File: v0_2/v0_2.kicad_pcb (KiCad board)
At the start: 2 copper layers, 36 x 70 mm, 46 parts, among them IC1 RASPBERRY_PI_PICO_W, IC2 BH1750FVI-TR, IC3 AP2138N-3.3TRG1, J1 S2B-PH-SM4-TB_LF__SN_, J2 HYCW110-TF10-180B, J3 Conn_01x09_Pin, Q1 DMG2301L-7, Q2 DMG2301L-7, Q3 DMG2301L-7, Q4 DMN3731U-13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

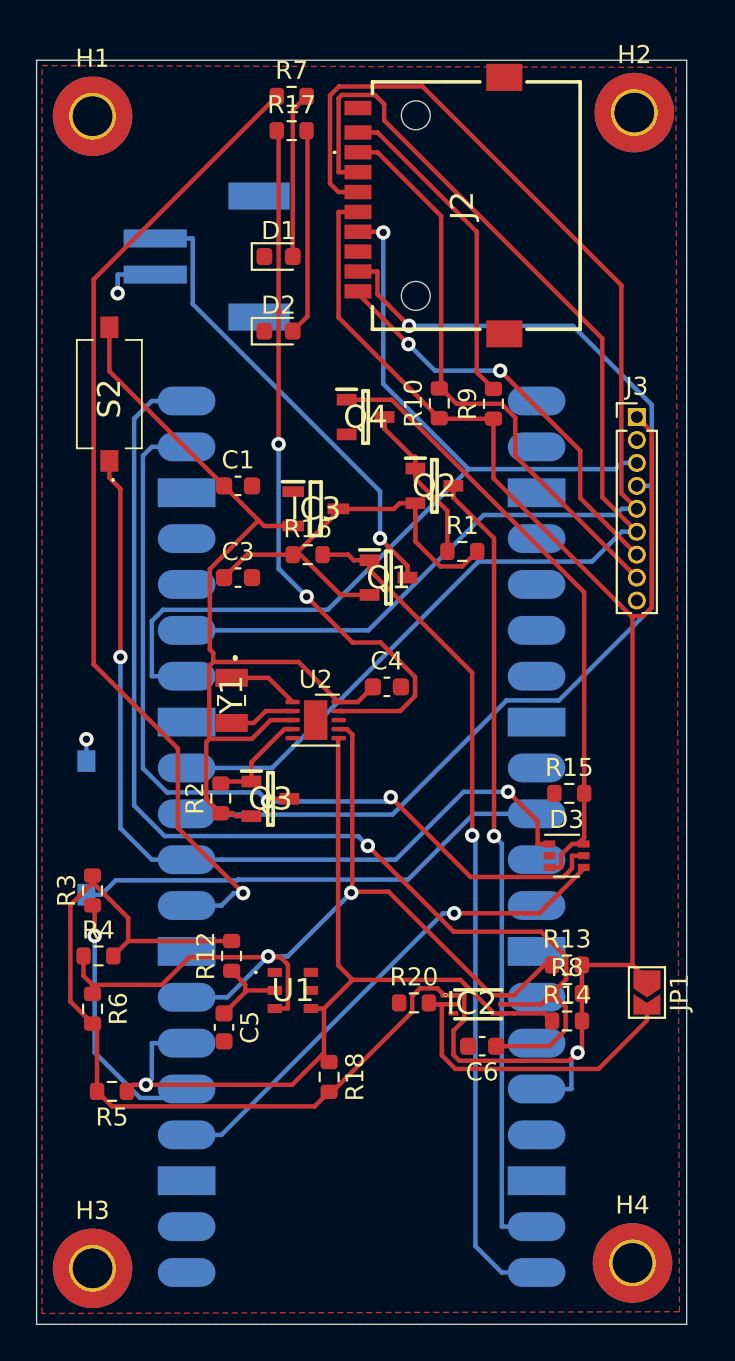
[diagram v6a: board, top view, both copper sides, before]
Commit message: rename i2c and add button
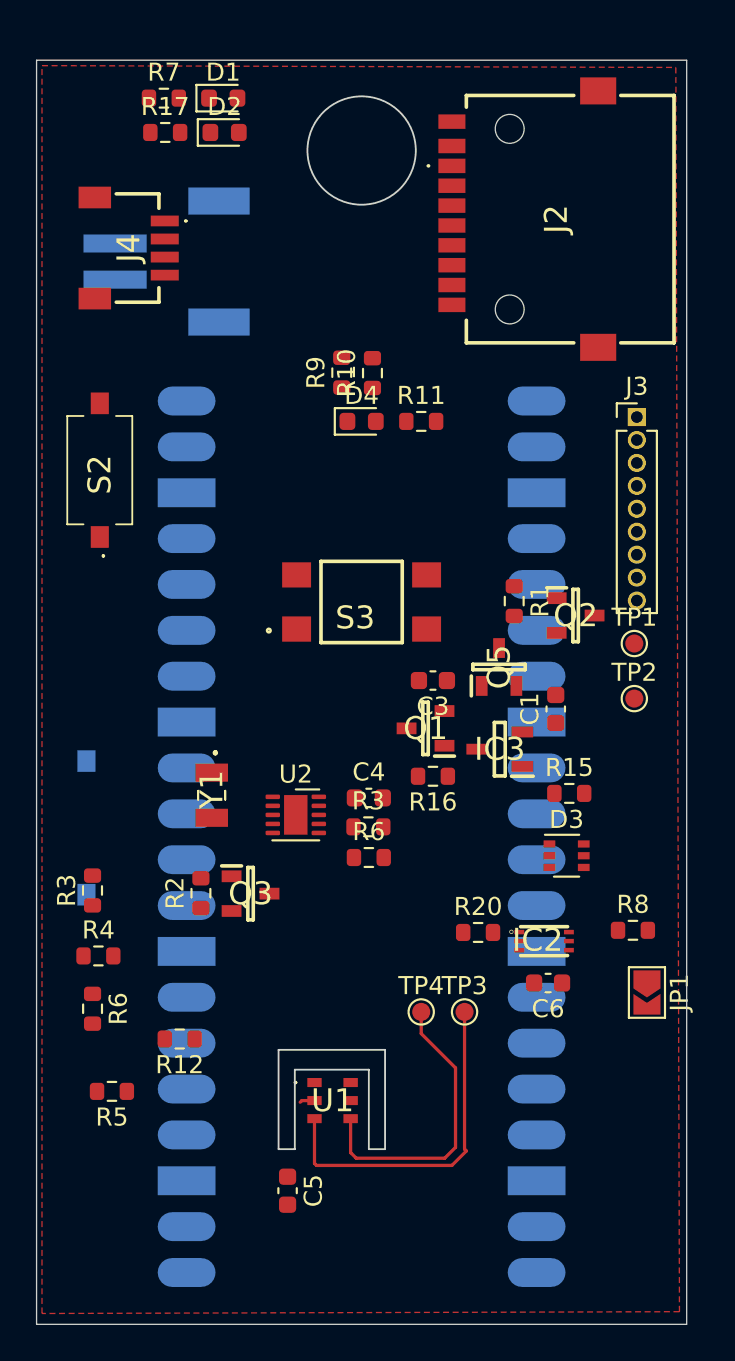
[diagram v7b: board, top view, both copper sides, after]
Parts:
- removed H1, H2, H3, H4: MountingHole_Pad, MountingHole:MountingHole_2.2mm_M2_Pad_TopBottom
- removed Q4: DMN3731U-13, DMN3731U-13:SOT96P240X110-3N
- removed R13, R14, R18: 10K, Resistor_SMD:R_0603_1608Metric
- added D4: RedLED, LED_SMD:LED_0603_1608Metric, F.Cu at (0.00, -15.0)
- added J4: SM04B-SRSS-TB, SM04B-SRSS-TB:SM04BSRSSTB, F.Cu at (-13.2, -24.6)
- added Q5: DMN3731U-7, DMN3731U-7:SOT96P240X110-3N, F.Cu at (7.61, -1.40)
- added R11: 1K, Resistor_SMD:R_0603_1608Metric, F.Cu at (3.30, -15.0)
- added R3: 10K, Resistor_SMD:R_0603_1608Metric, F.Cu at (0.38, 7.45)
- added R6: 10K, Resistor_SMD:R_0603_1608Metric, F.Cu at (0.40, 9.15)
- added S3: TL3305AF260QG, TL3305AF260QG:TL3305AF160QG, F.Cu at (0.00, -5.00)
- added TP1: TestPoint, TestPoint:TestPoint_Pad_D1.0mm, F.Cu at (15.1, -2.70)
- added TP2: TestPoint, TestPoint:TestPoint_Pad_D1.0mm, F.Cu at (15.1, 0.35)
- added TP3: TestPoint, TestPoint:TestPoint_Pad_D1.0mm, F.Cu at (5.70, 17.7)
- added TP4: TestPoint, TestPoint:TestPoint_Pad_D1.0mm, F.Cu at (3.30, 17.7)
- moved C1 21.5 mm to (10.8, 0.93), turned to 90 degrees
- moved IC3 16.8 mm to (7.65, 3.15), turned to 180 degrees
- moved R16 14.1 mm to (3.95, 4.65), turned to 180 degrees
- moved C3 12.2 mm to (3.95, -0.65), turned to 180 degrees
- moved D2 11.4 mm to (-7.59, -31.0)
- moved Q2 10.6 mm to (11.8, -4.25)
- moved C5 9.71 mm to (-4.10, 27.6)
- moved D1 9.29 mm to (-7.66, -32.9)
- moved Q1 8.60 mm to (3.54, 2.00), turned to 180 degrees
- moved R9 8.58 mm to (-1.10, -17.7)
- moved R7 7.08 mm to (-10.9, -32.9)
- moved R17 7.00 mm to (-10.9, -31.0)
- moved U1 6.48 mm to (-1.61, 22.6)
- moved C4 6.23 mm to (0.40, 5.85)
- moved R12 5.42 mm to (-10.1, 19.2), turned to 180 degrees
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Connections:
- net Net-(IC3-VIN) renamed /LDO/VIN
- IC1 pad 16: unconnected-(IC1-UART0_TX/I2C0_SDA_/SPI1_RX_/GP12-Pad16) -> /Record
- IC1 pad 21: unconnected-(IC1-UART0_TX/I2C0_SDA_/SPI0_RX_/GP16-Pad21) -> /I2C0_SDA
- IC1 pad 22: unconnected-(IC1-UART0_RX/I2C0_SCL/SPIO_CSN/GP17-Pad22) -> /I2C0_SCL
- IC1 pad 5: /I2C_INT/2.3B -> /Button
- IC1 pad 6: /I2C_SDA/2.1B -> /I2C1_SDA
- IC1 pad 7: /I2C_SCL/2.1B -> /I2C1_SCL
- IC2 pad 4: /I2C_SDA/2.1B -> /I2C1_SDA
- IC2 pad 6: /I2C_SCL/2.1B -> /I2C1_SCL
- J2 pad 10: Net-(J2-COM) -> /SDcard/CARDDET
- R3 pad 1: /I2C_INT/2.3B -> /I2C1_SCL
- R4 pad 1: /I2C_SCL/2.1B -> /I2C0_SCL
- R5 pad 1: /I2C_SDA/2.1B -> /I2C0_SDA
- R6 pad 1: /I2C_SCL/2.1B -> /I2C1_SDA
- R9 pad 2: Net-(J2-COM) -> /SDcard/CARDDET
- U1 pad 3: /I2C_SCL/2.1B -> /I2C1_SCL
- U1 pad 4: /I2C_SDA/2.1B -> /I2C1_SDA
- U2 pad 6: /I2C_SDA/2.1B -> /I2C1_SDA
- U2 pad 7: /I2C_SCL/2.1B -> /I2C1_SCL
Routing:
- net +3.3V: track 135.3 -> 0.00 mm, vias 1 -> 0
- net /MOSI: track 68.0 -> 0.00 mm
- net /CS: track 67.8 -> 0.00 mm
- net /RESET: track 64.0 -> 0.00 mm, vias 1 -> 0
- net /MISO: track 62.6 -> 0.00 mm, vias 1 -> 0
- net /ACT_LED: track 55.2 -> 0.00 mm, vias 1 -> 0
- net /I2C_SCL/2.1B: track 52.4 -> 0.00 mm, vias 2 -> 0
- net /SCK: track 51.9 -> 0.00 mm, vias 1 -> 0
- net V+_A0: track 51.0 -> 0.00 mm
- net /RTC_ALARM: track 49.2 -> 0.00 mm, vias 2 -> 0
- net /SWITCH_STATUS: track 48.6 -> 0.00 mm, vias 2 -> 0
- net /I2C_SDA/2.1B: track 47.9 -> 0.00 mm, vias 1 -> 0
- net VBUS: track 47.2 -> 0.00 mm, vias 1 -> 0
- net VSYS: track 44.1 -> 0.00 mm, vias 1 -> 0
- net /ALARM_LED: track 40.0 -> 0.00 mm, vias 2 -> 0
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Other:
- outline, holes or cut-outs redrawn

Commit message: add altoids case
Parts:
- moved C1 257.1 mm to (261.2, 58.9)
- moved C3 257.1 mm to (254.4, 57.3)
- moved C6 257.1 mm to (260.8, 74.1)
- moved D2 257.1 mm to (242.9, 27.0)
- moved J1 257.1 mm to (240.1, 34.1)
- moved J3 257.1 mm to (265.7, 42.7)
- moved J4 257.1 mm to (237.3, 33.4)
- moved Q1 257.1 mm to (254.0, 60.0)
- moved Q3 257.1 mm to (244.3, 69.1)
- moved R1 257.1 mm to (258.9, 52.9)
- moved R10 257.1 mm to (251.1, 40.3)
- moved R15 257.1 mm to (262.0, 63.6)
- moved R16 257.1 mm to (254.4, 62.6)
- moved R2 257.1 mm to (241.6, 69.1)
- moved R20 257.1 mm to (256.9, 71.3)
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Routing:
- net /I2C1_SCL: track 19.0 -> 16.5 mm
- net /I2C1_SDA: track 16.4 -> 14.5 mm
- net Net-(U1-VDD): track 0.83 -> 0.00 mm
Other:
- board size 36 x 70 mm -> 169.4 x 91.6 mm
